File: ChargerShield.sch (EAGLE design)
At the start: 23 parts, among them Q1 BD648, T2 BC548, X1 +5V, X2 Battery, X3 VCC

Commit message: added software and board
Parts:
- R5: device rcl:R-EU_0207/10 -> rcl:R-EU_0207/15
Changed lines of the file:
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@@
 <part name="T2" library="transistor" deviceset="BC238" device="" value="BC548"/>
 <part name="R4" library="rcl" deviceset="R-EU_" device="0207/10" value="2k2"/>
-<part name="R5" library="rcl" deviceset="R-EU_" device="0207/10" value="1k"/>
+<part name="R5" library="rcl" deviceset="R-EU_" device="0207/15" value="1k"/>
 <part name="C3" library="rcl" deviceset="C-EU" device="025_050-025X075" value="15n/60V"/>
 <part name="GND4" library="supply1" deviceset="GND" device=""/>

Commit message: current sense
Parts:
- added IC1: LM324N, linear:LM324N
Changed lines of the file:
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@@
 <setting verticaltext="up"/>
 </settings>
-<grid distance="0.05" unitdist="inch" unit="inch" style="lines" multiple="1" display="yes" altdistance="0.025" altunitdist="inch" altunit="inch"/>
+<grid distance="0.1" unitdist="inch" unit="inch" style="lines" multiple="1" display="no" altdistance="0.01" altunitdist="inch" altunit="inch"/>
 <layers>
-<layer number="1" name="Top" color="4" fill="1" visible="yes" active="no"/>
-<layer number="2" name="Route2" color="1" fill="3" visible="yes" active="no"/>
-<layer number="3" name="Route3" color="4" fill="3" visible="yes" active="no"/>
-<layer number="4" name="Route4" color="1" fill="4" visible="yes" active="no"/>
-<layer number="5" name="Route5" color="4" fill="4" visible="yes" active="no"/>
-<layer number="6" name="Route6" color="1" fill="8" visible="yes" active="no"/>
-<layer number="7" name="Route7" color="4" fill="8" visible="yes" active="no"/>
-<layer number="8" name="Route8" color="1" fill="2" visible="yes" active="no"/>
-<layer number="9" name="Route9" color="4" fill="2" visible="yes" active="no"/>
-<layer number="10" name="Route10" color="1" fill="7" visible="yes" active="no"/>
-<layer number="11" name="Route11" color="4" fill="7" visible="yes" active="no"/>
-<layer number="12" name="Route12" color="1" fill="5" visible="yes" active="no"/>
-<layer number="13" name="Route13" color="4" fill="5" visible="yes" active="no"/>
-<layer number="14" name="Route14" color="1" fill="6" visible="yes" active="no"/>
-<layer number="15" name="Route15" color="4" fill="6" visible="yes" active="no"/>
-<layer number="16" name="Bottom" color="1" fill="1" visible="yes" active="no"/>
-<layer number="17" name="Pads" color="2" fill="1" visible="yes" active="no"/>
-<layer number="18" name="Vias" color="2" fill="1" visible="yes" active="no"/>
-<layer number="19" name="Unrouted" color="6" fill="1" visible="yes" active="no"/>
-<layer number="20" name="Dimension" color="15" fill="1" visible="yes" active="no"/>
-<layer number="21" name="tPlace" color="7" fill="1" visible="yes" active="no"/>
-<layer number="22" name="bPlace" color="7" fill="1" visible="yes" active="no"/>
-<layer number="23" name="tOrigins" color="15" fill="1" visible="yes" active="no"/>
-<layer number="24" name="bOrigins" color="15" fill="1" visible="yes" active="no"/>
-<layer number="25" name="tNames" color="7" fill="1" visible="yes" active="no"/>
-<layer number="26" name="bNames" color="7" fill="1" visible="yes" active="no"/>
-<layer number="27" name="tValues" color="7" fill="1" visible="yes" active="no"/>
-<layer number="28" name="bValues" color="7" fill="1" visible="yes" active="no"/>
+<layer number="1" name="Top" color="4" fill="1" visible="no" active="no"/>
+<layer number="2" name="Route2" color="1" fill="3" visible="no" active="no"/>
+<layer number="3" name="Route3" color="4" fill="3" visible="no" active="no"/>
+<layer number="4" name="Route4" color="1" fill="4" visible="no" active="no"/>
+<layer number="5" name="Route5" color="4" fill="4" visible="no" active="no"/>
+<layer number="6" name="Route6" color="1" fill="8" visible="no" active="no"/>
+<layer number="7" name="Route7" color="4" fill="8" visible="no" active="no"/>
+<layer number="8" name="Route8" color="1" fill="2" visible="no" active="no"/>
+<layer number="9" name="Route9" color="4" fill="2" visible="no" active="no"/>
+<layer number="10" name="Route10" color="1" fill="7" visible="no" active="no"/>
+<layer number="11" name="Route11" color="4" fill="7" visible="no" active="no"/>
+<layer number="12" name="Route12" color="1" fill="5" visible="no" active="no"/>
+<layer number="13" name="Route13" color="4" fill="5" visible="no" active="no"/>
+<layer number="14" name="Route14" color="1" fill="6" visible="no" active="no"/>
+<layer number="15" name="Route15" color="4" fill="6" visible="no" active="no"/>
+<layer number="16" name="Bottom" color="1" fill="1" visible="no" active="no"/>
+<layer number="17" name="Pads" color="2" fill="1" visible="no" active="no"/>
+<layer number="18" name="Vias" color="2" fill="1" visible="no" active="no"/>
+<layer number="19" name="Unrouted" color="6" fill="1" visible="no" active="no"/>
+<layer number="20" name="Dimension" color="15" fill="1" visible="no" active="no"/>
+<layer number="21" name="tPlace" color="7" fill="1" visible="no" active="no"/>
+<layer number="22" name="bPlace" color="7" fill="1" visible="no" active="no"/>
+<layer number="23" name="tOrigins" color="15" fill="1" visible="no" active="no"/>
+<layer number="24" name="bOrigins" color="15" fill="1" visible="no" active="no"/>
+<layer number="25" name="tNames" color="7" fill="1" visible="no" active="no"/>
+<layer number="26" name="bNames" color="7" fill="1" visible="no" active="no"/>
+<layer number="27" name="tValues" color="7" fill="1" visible="no" active="no"/>
+<layer number="28" name="bValues" color="7" fill="1" visible="no" active="no"/>
 <layer number="29" name="tStop" color="7" fill="3" visible="no" active="no"/>
 <layer number="30" name="bStop" color="7" fill="6" visible="no" active="no"/>
@@
 <layer number="35" name="tGlue" color="7" fill="4" visible="no" active="no"/>
 <layer number="36" name="bGlue" color="7" fill="5" visible="no" active="no"/>
-<layer number="37" name="tTest" color="7" fill="1" visible="yes" active="no"/>
-<layer number="38" name="bTest" color="7" fill="1" visible="yes" active="no"/>
+<layer number="37" name="tTest" color="7" fill="1" visible="no" active="no"/>
+<layer number="38" name="bTest" color="7" fill="1" visible="no" active="no"/>
 <layer number="39" name="tKeepout" color="4" fill="11" visible="no" active="no"/>
 <layer number="40" name="bKeepout" color="1" fill="11" visible="no" active="no"/>
@@
 <layer number="44" name="Drills" color="7" fill="1" visible="no" active="no"/>
 <layer number="45" name="Holes" color="7" fill="1" visible="no" active="no"/>
-<layer number="46" name="Milling" color="3" fill="1" visible="yes" active="no"/>
-<layer number="47" name="Measures" color="7" fill="1" visible="yes" active="no"/>
-<layer number="48" name="Document" color="7" fill="1" visible="yes" active="no"/>
-<layer number="49" name="Reference" color="7" fill="1" visible="yes" active="no"/>
-<layer number="50" name="dxf" color="7" fill="1" visible="yes" active="no"/>
-<layer number="51" name="tDocu" color="7" fill="1" visible="yes" active="no"/>
-<layer number="52" name="bDocu" color="7" fill="1" visible="yes" active="no"/>
-<layer number="53" name="tGND_GNDA" color="7" fill="9" visible="yes" active="no"/>
-<layer number="54" name="bGND_GNDA" color="1" fill="9" visible="yes" active="no"/>
-<layer number="56" name="wert" color="7" fill="1" visible="yes" active="no"/>
-<layer number="57" name="tCAD" color="7" fill="1" visible="yes" active="no"/>
+<layer number="46" name="Milling" color="3" fill="1" visible="no" active="no"/>
+<layer number="47" name="Measures" color="7" fill="1" visible="no" active="no"/>
+<layer number="48" name="Document" color="7" fill="1" visible="no" active="no"/>
+<layer number="49" name="Reference" color="7" fill="1" visible="no" active="no"/>
+<layer number="50" name="dxf" color="7" fill="1" visible="no" active="no"/>
+<layer number="51" name="tDocu" color="7" fill="1" visible="no" active="no"/>
+<layer number="52" name="bDocu" color="7" fill="1" visible="no" active="no"/>
+<layer number="53" name="tGND_GNDA" color="7" fill="9" visible="no" active="no"/>
+<layer number="54" name="bGND_GNDA" color="1" fill="9" visible="no" active="no"/>
+<layer number="56" name="wert" color="7" fill="1" visible="no" active="no"/>
+<layer number="57" name="tCAD" color="7" fill="1" visible="no" active="no"/>
 <layer number="91" name="Nets" color="2" fill="1" visible="yes" active="yes"/>
 <layer number="92" name="Busses" color="1" fill="1" visible="yes" active="yes"/>
@@
 <part name="X3" library="con-wago-500" deviceset="W237-102" device="" value="VCC"/>
 <part name="P+4" library="supply1" deviceset="VCC" device=""/>
+<part name="IC1" library="linear" deviceset="LM324" device="N"/>
 </parts>
 <sheets>
@@
 <instance part="X3" gate="-2" x="64.77" y="146.05"/>
 <instance part="P+4" gate="VCC" x="74.93" y="158.75"/>
+<instance part="IC1" gate="A" x="73.66" y="63.5"/>
 </instances>
 <busses>

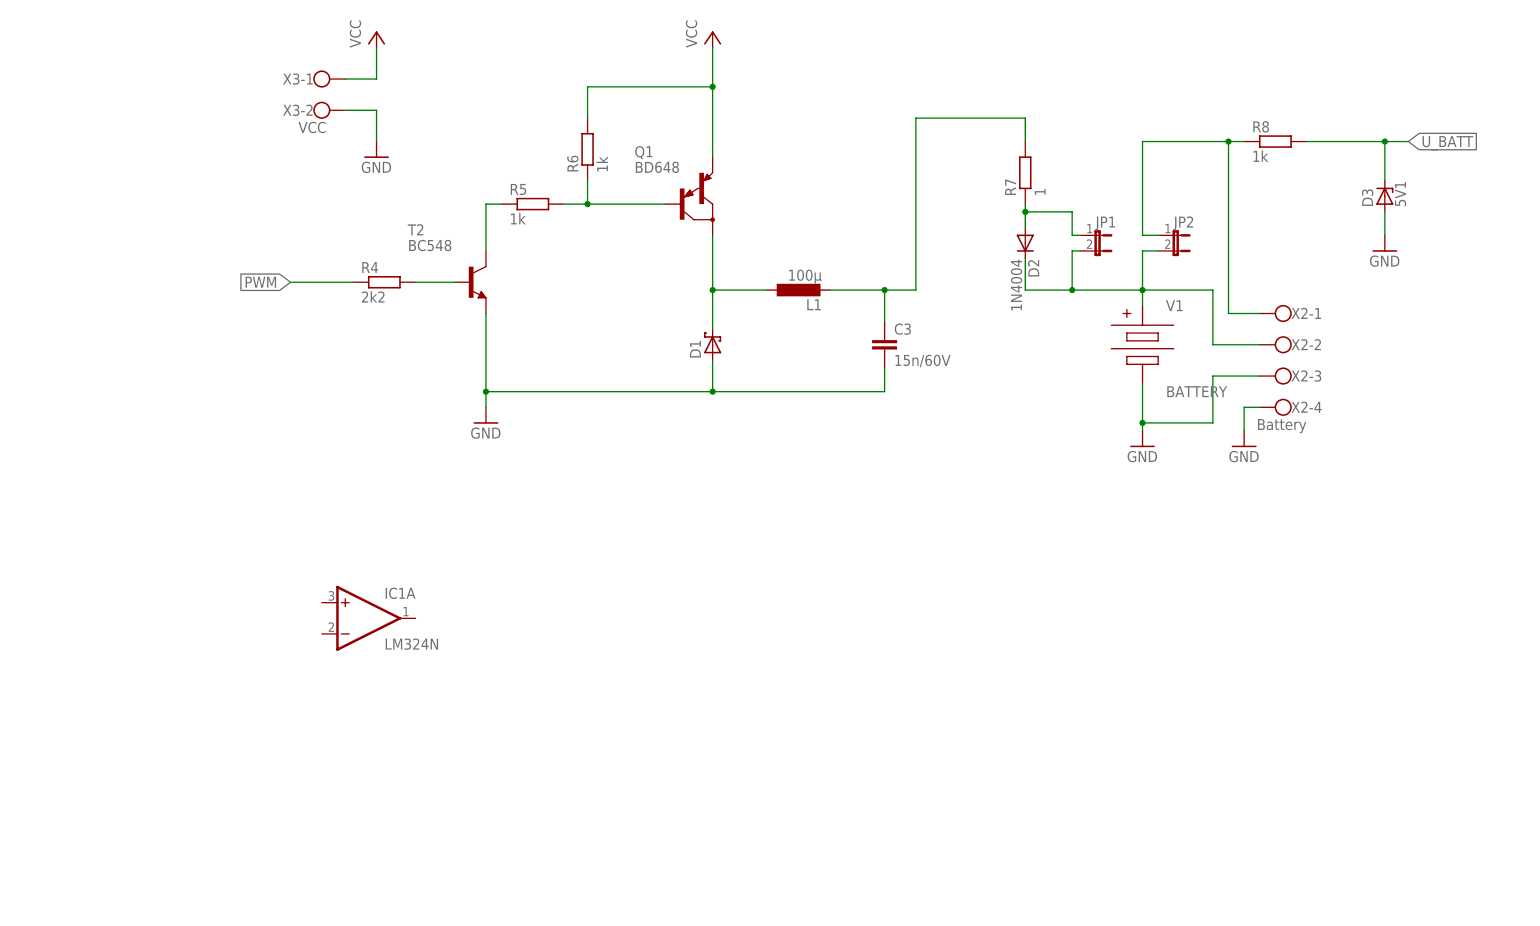
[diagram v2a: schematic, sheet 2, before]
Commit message: start button and current sense program
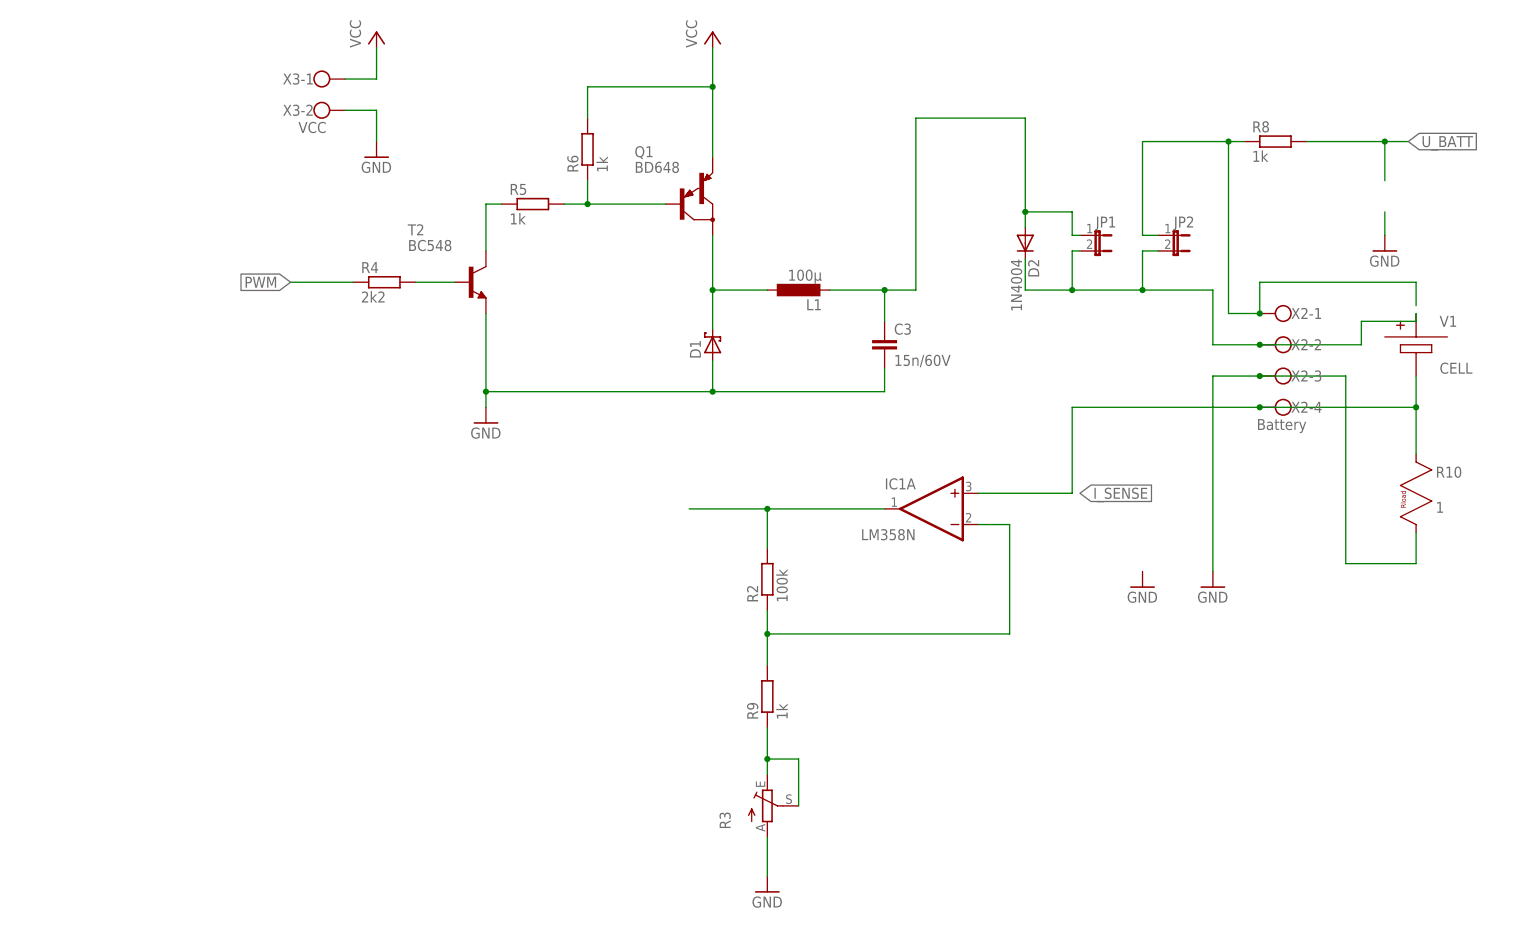
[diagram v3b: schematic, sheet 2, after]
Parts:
- removed D3: 5V1, diode:ZPD
- removed R7: 1, rcl:R-EU_0617/22
- added R10: 1, lt-spice-simulation:RES_RLOAD
- added R2: 100k, rcl:R-EU_0207/10
- added R3: (no value), pot:TRIM_EU-LI10
- added R9: 1k, rcl:R-EU_0207/10
- IC1: value LM324N -> LM358N; device linear:LM324N -> linear:LM358N
- V1: value BATTERY -> CELL; device Misc:BATTERY -> Misc:CELL
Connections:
- new net I_SENSE: IC1A.+IN, R10.A, V1.-, X2-4.KL
- new net N$14: IC1A.-IN, R2.1, R9.2
- new net N$15: R3.E, R3.S, R9.1
- net GND: now also R10.B, R3.A; no longer D3.A, V1.-, X2-4.KL
- net N$10: now also D2.A, JP1.1; no longer R7.2
- net N$11: now also IC1A.OUT, R2.2; no longer D2.A, JP1.1, R7.1
- net U_BATT: no longer D3.C
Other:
- moved on the sheet: IC1A

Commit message: smaller diode
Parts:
- D1: device diode:SCHOTTKY-DIODEC4111-15 -> diode:SCHOTTKY-DIODEDO35-7
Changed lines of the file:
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@@
 <part name="R6" library="rcl" deviceset="R-EU_" device="0207/10" value="1k"/>
 <part name="Q1" library="transistor-pnp" deviceset="BD648" device=""/>
-<part name="D1" library="diode" deviceset="SCHOTTKY-DIODE" device="C4111-15"/>
+<part name="D1" library="diode" deviceset="SCHOTTKY-DIODE" device="DO35-7"/>
 <part name="L1" library="rcl" deviceset="L-EU" device="0207/12" value="100µ"/>
 <part name="V1" library="Misc" deviceset="CELL" device=""/>

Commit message: Discharge
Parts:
- added Q2: BD648, transistor-pnp:BD648
- added R7: 1, rcl:R-EU_0414/15
- R10: value 1 -> 0R15
- R3: value (none) -> 10k
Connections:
- new net N$12: Q2.C, R7.2
- net GND: now also R7.1
- net N$13: now also Q2.E
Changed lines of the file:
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@@
 <part name="IC1" library="linear" deviceset="LM358" device="N"/>
 <part name="R2" library="rcl" deviceset="R-EU_" device="0207/10" value="100k"/>
-<part name="R3" library="pot" deviceset="TRIM_EU-" device="LI10"/>
+<part name="R3" library="pot" deviceset="TRIM_EU-" device="LI10" value="10k"/>
 <part name="R9" library="rcl" deviceset="R-EU_" device="0207/10" value="1k"/>
 <part name="GND9" library="supply1" deviceset="GND" device=""/>
-<part name="R10" library="lt-spice-simulation" deviceset="RES_RLOAD" device="" value="1"/>
+<part name="R10" library="lt-spice-simulation" deviceset="RES_RLOAD" device="" value="0R15"/>
+<part name="R7" library="rcl" deviceset="R-EU_" device="0414/15" value="1"/>
+<part name="Q2" library="transistor-pnp" deviceset="BD648" device=""/>
+<part name="GND10" library="supply1" deviceset="GND" device=""/>
 </parts>
 <sheets>
@@
 <instance part="GND9" gate="1" x="138.43" y="19.05"/>
 <instance part="R10" gate="G$1" x="241.3" y="92.71"/>
+<instance part="R7" gate="G$1" x="68.58" y="35.56" rot="R90"/>
+<instance part="Q2" gate="G$1" x="63.5" y="82.55"/>
+<instance part="GND10" gate="1" x="68.58" y="19.05"/>
 </instances>
 <busses>
@@
 <pinref part="R10" gate="G$1" pin="B"/>
 </segment>
+<segment>
+<pinref part="R7" gate="G$1" pin="1"/>
+<pinref part="GND10" gate="1" pin="GND"/>
+<wire x1="68.58" y1="30.48" x2="68.58" y2="21.59" width="0.1524" layer="91"/>
+</segment>
 </net>
 <net name="N$6" class="0">
@@
 <junction x="157.48" y="116.84"/>
 <wire x1="157.48" y1="116.84" x2="162.56" y2="116.84" width="0.1524" layer="91"/>
-<wire x1="162.56" y1="116.84" x2="162.56" y2="144.78" width="0.1524" layer="91"/>
+<wire x1="162.56" y1="116.84" x2="162.56" y2="129.54" width="0.1524" layer="91"/>
 <pinref part="D2" gate="1" pin="A"/>
 <pinref part="JP1" gate="A" pin="1"/>
@@
 <wire x1="187.96" y1="125.73" x2="187.96" y2="129.54" width="0.1524" layer="91"/>
 <wire x1="187.96" y1="129.54" x2="180.34" y2="129.54" width="0.1524" layer="91"/>
-<wire x1="162.56" y1="144.78" x2="180.34" y2="144.78" width="0.1524" layer="91"/>
-<wire x1="180.34" y1="144.78" x2="180.34" y2="129.54" width="0.1524" layer="91"/>
+<wire x1="162.56" y1="129.54" x2="180.34" y2="129.54" width="0.1524" layer="91"/>
 <junction x="180.34" y="129.54"/>
 </segment>
@@
 <pinref part="V1" gate="G$1" pin="+"/>
 <wire x1="243.84" y1="111.76" x2="243.84" y2="113.03" width="0.1524" layer="91"/>
+<wire x1="210.82" y1="107.95" x2="180.34" y2="107.95" width="0.1524" layer="91"/>
+<junction x="210.82" y="107.95"/>
+<wire x1="180.34" y1="107.95" x2="180.34" y2="91.44" width="0.1524" layer="91"/>
+<wire x1="180.34" y1="91.44" x2="68.58" y2="91.44" width="0.1524" layer="91"/>
+<pinref part="Q2" gate="G$1" pin="E"/>
+<wire x1="68.58" y1="91.44" x2="68.58" y2="90.17" width="0.1524" layer="91"/>
 </segment>
 </net>
@@
 </segment>
 </net>
+<net name="N$12" class="0">
+<segment>
+<pinref part="Q2" gate="G$1" pin="C"/>
+<pinref part="R7" gate="G$1" pin="2"/>
+<wire x1="68.58" y1="77.47" x2="68.58" y2="40.64" width="0.1524" layer="91"/>
+</segment>
+</net>
